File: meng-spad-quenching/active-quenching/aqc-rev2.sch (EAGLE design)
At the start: 289 parts, among them IC1 ADCMP582, IC10 74AHC1G04DBV, IC11 74AHC1G04DBV, IC12 TLV272DGK, IC13 TLV271DBV, IC14 74AHC1G04DBV, IC15 ALD1106, IC16 ALD1107, IC17 74AHC1G04DBV, IC18 LT1534-1, IC19 LT1534-1, IC2 TLV271DBV, IC20 STM32F411RE, IC22 TPS7A3001, IC24 TPS7A4901, IC25 TPS7A4901, IC27 USBLC6-2SC6Y, IC28 MAX572X, IC3 NC7SV74K8X, IC4 TLV272DGK, IC5 NC7WZ16P6X, IC6 LTC1711, IC7 DS1100LU-20+, IC8 LM1117, M1 BSS806N, M2 BSS806N, M3 BSS806N, Q1 IRLML6402TRPBF, Q2 MMBTH81, Q3 MMBTH81, Q5 MMBTH81, Q7 MMBTH81, Q8 MMBTH81, T1 MMBTH10, T2 MMBTH10, T5 MMBTH10, T6 MMBTH10, T7 MMBTH10, T8 MMBTH10, T9 MMBTH10, U1 SN65EPT21DGK, U2 SN65EPT22DGK, X1 CONN_SPAD, X2 CONN_PHOTON_COUNTER, X3 KEYSTONE-7774, X4 KEYSTONE-7774, X5 CONN_SMU, X6 CONN_FORCE_QUENCH, X7 CONN_PULLDN_SENSE, X8 PN61729-S

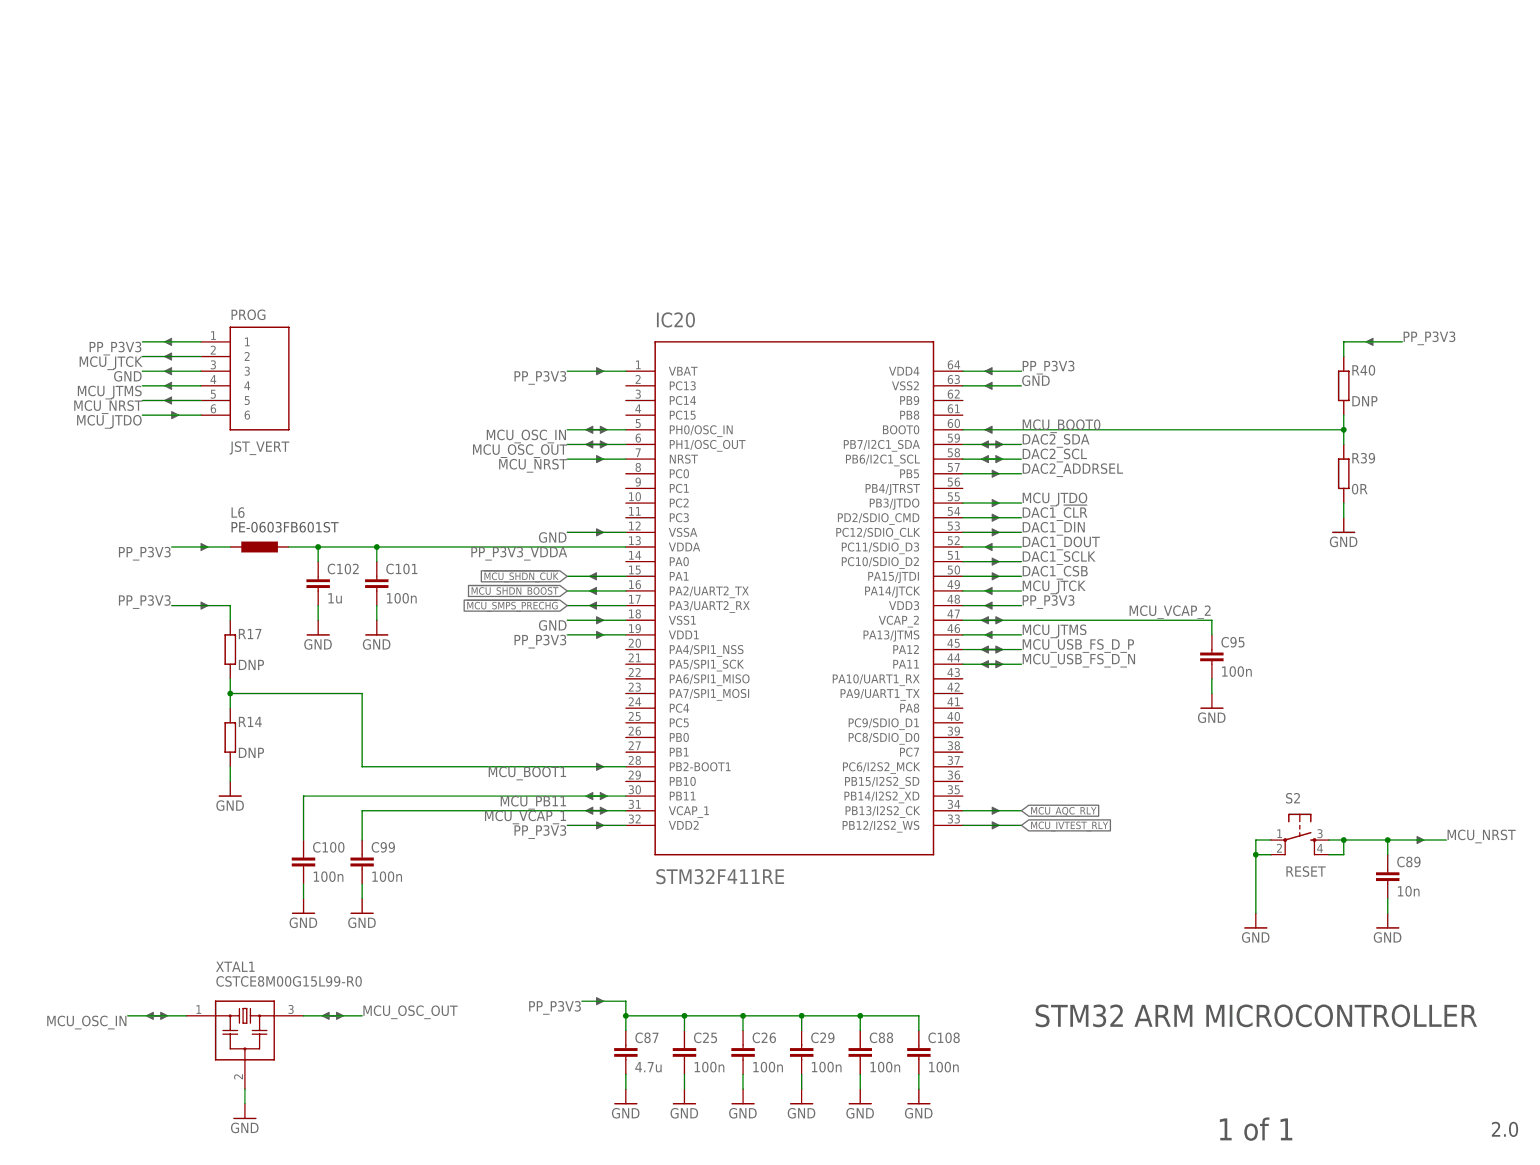
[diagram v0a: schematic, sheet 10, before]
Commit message: Untangled DAC test points
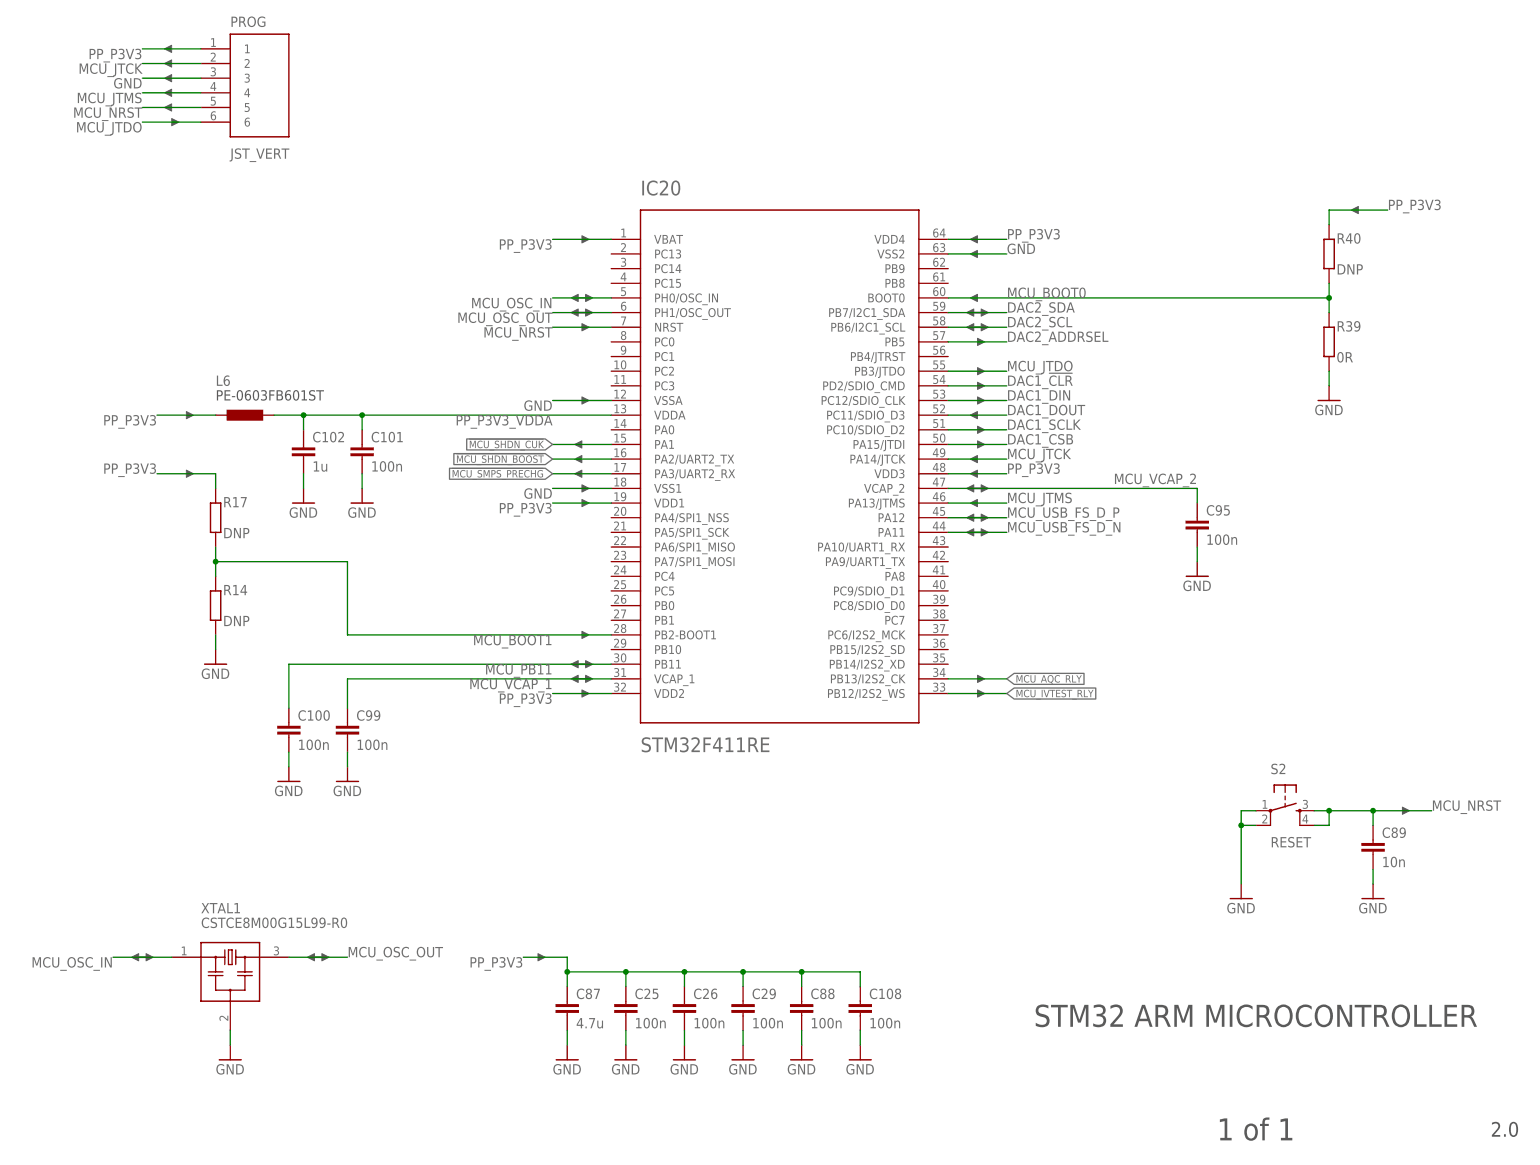
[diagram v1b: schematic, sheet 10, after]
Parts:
- TP10: value VREF_CASCODE_IBIAS -> CASC_IBIAS
- TP11: value VREF_DIAMOND_IBIAS -> DMND_IBIAS
- TP12: value VREF_ONE_SHOT -> ONE_SHOT
- TP15: value VREF_SLEW_UP -> SLEW_UP
- TP16: value VREF_SLEW_DN -> SLEW_DN
- TP17: value VREF_SLEW_MAX -> SLEW_MAX
- TP18: value VREF_DELAY_UP -> DELAY_UP
- TP19: value VREF_DELAY_DN -> DELAY_DN
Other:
- moved on the sheet: C100, C101, C102, C108, C25, C26, C29, C87, C88, C89, C95, C99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

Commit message: Transistor array routing
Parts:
- R37: device resistor:R-EU_R0805 -> resistor:R-EU_R0603
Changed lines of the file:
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@@
 <grid distance="0.1" unitdist="inch" unit="inch" style="lines" multiple="1" display="yes" altdistance="0.01" altunitdist="inch" altunit="inch"/>
 <layers>
-<layer number="1" name="Top" color="4" fill="1" visible="no" active="no"/>
-<layer number="2" name="Route2" color="3" fill="1" visible="no" active="no"/>
-<layer number="3" name="Route3" color="4" fill="3" visible="no" active="no"/>
-<layer number="4" name="Route4" color="1" fill="4" visible="no" active="no"/>
-<layer number="5" name="Route5" color="4" fill="4" visible="no" active="no"/>
-<layer number="6" name="Route6" color="1" fill="8" visible="no" active="no"/>
-<layer number="7" name="Route7" color="4" fill="8" visible="no" active="no"/>
-<layer number="8" name="Route8" color="1" fill="2" visible="no" active="no"/>
-<layer number="9" name="Route9" color="4" fill="2" visible="no" active="no"/>
-<layer number="10" name="Route10" color="1" fill="7" visible="no" active="no"/>
-<layer number="11" name="Route11" color="4" fill="7" visible="no" active="no"/>
-<layer number="12" name="Route12" color="1" fill="5" visible="no" active="no"/>
-<layer number="13" name="Route13" color="4" fill="5" visible="no" active="no"/>
-<layer number="14" name="Route14" color="1" fill="6" visible="no" active="no"/>
-<layer number="15" name="Route15" color="6" fill="1" visible="no" active="no"/>
-<layer number="16" name="Bottom" color="1" fill="1" visible="no" active="no"/>
-<layer number="17" name="Pads" color="2" fill="1" visible="no" active="no"/>
-<layer number="18" name="Vias" color="2" fill="1" visible="no" active="no"/>
-<layer number="19" name="Unrouted" color="6" fill="1" visible="no" active="no"/>
-<layer number="20" name="Dimension" color="15" fill="1" visible="no" active="no"/>
-<layer number="21" name="tPlace" color="7" fill="1" visible="no" active="no"/>
-<layer number="22" name="bPlace" color="7" fill="1" visible="no" active="no"/>
-<layer number="23" name="tOrigins" color="15" fill="1" visible="no" active="no"/>
-<layer number="24" name="bOrigins" color="15" fill="1" visible="no" active="no"/>
-<layer number="25" name="tNames" color="7" fill="1" visible="no" active="no"/>
-<layer number="26" name="bNames" color="7" fill="1" visible="no" active="no"/>
-<layer number="27" name="tValues" color="7" fill="1" visible="no" active="no"/>
-<layer number="28" name="bValues" color="7" fill="1" visible="no" active="no"/>
+<layer number="1" name="Top" color="4" fill="1" visible="yes" active="no"/>
+<layer number="2" name="Route2" color="3" fill="1" visible="yes" active="no"/>
+<layer number="3" name="Route3" color="4" fill="3" visible="yes" active="no"/>
+<layer number="4" name="Route4" color="1" fill="4" visible="yes" active="no"/>
+<layer number="5" name="Route5" color="4" fill="4" visible="yes" active="no"/>
+<layer number="6" name="Route6" color="1" fill="8" visible="yes" active="no"/>
+<layer number="7" name="Route7" color="4" fill="8" visible="yes" active="no"/>
+<layer number="8" name="Route8" color="1" fill="2" visible="yes" active="no"/>
+<layer number="9" name="Route9" color="4" fill="2" visible="yes" active="no"/>
+<layer number="10" name="Route10" color="1" fill="7" visible="yes" active="no"/>
+<layer number="11" name="Route11" color="4" fill="7" visible="yes" active="no"/>
+<layer number="12" name="Route12" color="1" fill="5" visible="yes" active="no"/>
+<layer number="13" name="Route13" color="4" fill="5" visible="yes" active="no"/>
+<layer number="14" name="Route14" color="1" fill="6" visible="yes" active="no"/>
+<layer number="15" name="Route15" color="6" fill="1" visible="yes" active="no"/>
+<layer number="16" name="Bottom" color="1" fill="1" visible="yes" active="no"/>
+<layer number="17" name="Pads" color="2" fill="1" visible="yes" active="no"/>
+<layer number="18" name="Vias" color="2" fill="1" visible="yes" active="no"/>
+<layer number="19" name="Unrouted" color="6" fill="1" visible="yes" active="no"/>
+<layer number="20" name="Dimension" color="15" fill="1" visible="yes" active="no"/>
+<layer number="21" name="tPlace" color="7" fill="1" visible="yes" active="no"/>
+<layer number="22" name="bPlace" color="7" fill="1" visible="yes" active="no"/>
+<layer number="23" name="tOrigins" color="15" fill="1" visible="yes" active="no"/>
+<layer number="24" name="bOrigins" color="15" fill="1" visible="yes" active="no"/>
+<layer number="25" name="tNames" color="7" fill="1" visible="yes" active="no"/>
+<layer number="26" name="bNames" color="7" fill="1" visible="yes" active="no"/>
+<layer number="27" name="tValues" color="7" fill="1" visible="yes" active="no"/>
+<layer number="28" name="bValues" color="7" fill="1" visible="yes" active="no"/>
 <layer number="29" name="tStop" color="7" fill="3" visible="no" active="no"/>
 <layer number="30" name="bStop" color="7" fill="6" visible="no" active="no"/>
@@
 <layer number="35" name="tGlue" color="7" fill="4" visible="no" active="no"/>
 <layer number="36" name="bGlue" color="7" fill="5" visible="no" active="no"/>
-<layer number="37" name="tTest" color="7" fill="1" visible="no" active="no"/>
-<layer number="38" name="bTest" color="7" fill="1" visible="no" active="no"/>
+<layer number="37" name="tTest" color="7" fill="1" visible="yes" active="no"/>
+<layer number="38" name="bTest" color="7" fill="1" visible="yes" active="no"/>
 <layer number="39" name="tKeepout" color="4" fill="11" visible="no" active="no"/>
 <layer number="40" name="bKeepout" color="1" fill="11" visible="no" active="no"/>
@@
 <layer number="44" name="Drills" color="7" fill="1" visible="no" active="no"/>
 <layer number="45" name="Holes" color="7" fill="1" visible="no" active="no"/>
-<layer number="46" name="Milling" color="3" fill="1" visible="no" active="no"/>
-<layer number="47" name="Measures" color="7" fill="1" visible="no" active="no"/>
-<layer number="48" name="Document" color="7" fill="1" visible="no" active="no"/>
-<layer number="49" name="Reference" color="7" fill="1" visible="no" active="no"/>
-<layer number="50" name="dxf" color="7" fill="1" visible="no" active="no"/>
-<layer number="51" name="tDocu" color="7" fill="1" visible="no" active="no"/>
-<layer number="52" name="bDocu" color="7" fill="1" visible="no" active="no"/>
-<layer number="53" name="tPadExt" color="7" fill="1" visible="no" active="no"/>
-<layer number="54" name="bPadExt" color="1" fill="1" visible="no" active="no"/>
-<layer number="56" name="wert" color="7" fill="1" visible="no" active="no"/>
-<layer number="57" name="tCAD" color="7" fill="1" visible="no" active="no"/>
-<layer number="59" name="tCarbon" color="7" fill="1" visible="no" active="no"/>
-<layer number="60" name="bCarbon" color="7" fill="1" visible="no" active="no"/>
+<layer number="46" name="Milling" color="3" fill="1" visible="yes" active="no"/>
+<layer number="47" name="Measures" color="7" fill="1" visible="yes" active="no"/>
+<layer number="48" name="Document" color="7" fill="1" visible="yes" active="no"/>
+<layer number="49" name="Reference" color="7" fill="1" visible="yes" active="no"/>
+<layer number="50" name="dxf" color="7" fill="1" visible="yes" active="no"/>
+<layer number="51" name="tDocu" color="7" fill="1" visible="yes" active="no"/>
+<layer number="52" name="bDocu" color="7" fill="1" visible="yes" active="no"/>
+<layer number="53" name="tPadExt" color="7" fill="1" visible="yes" active="no"/>
+<layer number="54" name="bPadExt" color="1" fill="1" visible="yes" active="no"/>
+<layer number="56" name="wert" color="7" fill="1" visible="yes" active="no"/>
+<layer number="57" name="tCAD" color="7" fill="1" visible="yes" active="no"/>
+<layer number="59" name="tCarbon" color="7" fill="1" visible="yes" active="no"/>
+<layer number="60" name="bCarbon" color="7" fill="1" visible="yes" active="no"/>
 <layer number="90" name="Modules" color="5" fill="1" visible="no" active="no"/>
 <layer number="91" name="Nets" color="2" fill="1" visible="yes" active="yes"/>
@@
 <part name="LED2" library="led" deviceset="LED" device="CHIP-LED0805"/>
 <part name="GND83" library="supply1" deviceset="GND" device=""/>
-<part name="R37" library="resistor" deviceset="R-EU_" device="R0805" value="470R"/>
+<part name="R37" library="resistor" deviceset="R-EU_" device="R0603" value="470R"/>
 <part name="TP12" library="Kramnik's Library" deviceset="KEYSTONE_5000" device="" value="ONE_SHOT"/>
 <part name="TP11" library="Kramnik's Library" deviceset="KEYSTONE_5000" device="" value="DMND_IBIAS"/>

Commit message: Added new SMA conns. w/o dimension edge line
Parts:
- X1, X2, X5, X6, X7: device con-coax:SMA-142-0711-871/876 -> meng:SMA-142-0711-871/876
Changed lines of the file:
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@@
 <part name="GND2" library="supply1" deviceset="GND" device=""/>
 <part name="R15" library="rcl" deviceset="R-EU_" device="R0603" value="10k"/>
-<part name="X1" library="con-coax" deviceset="SMA-" device="142-0711-871/876" value="CONN_SPAD"/>
-<part name="X2" library="con-coax" deviceset="SMA-" device="142-0711-871/876" value="CONN_PHOTON_COUNTER"/>
+<part name="X1" library="meng" deviceset="SMA-" device="142-0711-871/876" value="CONN_SPAD"/>
+<part name="X2" library="meng" deviceset="SMA-" device="142-0711-871/876" value="CONN_PHOTON_COUNTER"/>
 <part name="GND5" library="supply1" deviceset="GND" device=""/>
 <part name="DNP4" library="meng" deviceset="ARROW_1DIR" device=""/>
@@
 <part name="R22" library="rcl" deviceset="R-EU_" device="R0603" value="49R9"/>
 <part name="DNP67" library="meng" deviceset="ARROW_1DIR" device=""/>
-<part name="X6" library="con-coax" deviceset="SMA-" device="142-0711-871/876" value="CONN_FORCE_QUENCH">
+<part name="X6" library="meng" deviceset="SMA-" device="142-0711-871/876" value="CONN_FORCE_QUENCH">
 <attribute name="MF" value="JOHNSON COMPONENTS"/>
 <attribute name="MPN" value="142-0711-871"/>
@@
 <part name="R45" library="rcl" deviceset="R-EU_" device="R0603" value="DNP"/>
 <part name="R46" library="rcl" deviceset="R-EU_" device="R0603" value="0R"/>
-<part name="X7" library="con-coax" deviceset="SMA-" device="142-0711-871/876" value="CONN_PULLDN_SENSE">
+<part name="X7" library="meng" deviceset="SMA-" device="142-0711-871/876" value="CONN_PULLDN_SENSE">
 <attribute name="MF" value="JOHNSON COMPONENTS"/>
 <attribute name="MPN" value="142-0711-871"/>
@@
 <part name="GND161" library="supply1" deviceset="GND" device=""/>
 <part name="GND162" library="supply1" deviceset="GND" device=""/>
-<part name="X5" library="con-coax" deviceset="SMA-" device="142-0711-871/876" value="CONN_SMU"/>
+<part name="X5" library="meng" deviceset="SMA-" device="142-0711-871/876" value="CONN_SMU"/>
 <part name="GND163" library="supply1" deviceset="GND" device=""/>
 <part name="R70" library="rcl" deviceset="R-EU_" device="R0603" value="0R"/>

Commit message: Place & route diamond bias opamp
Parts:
- C82: device rcl:C-EUC0402 -> rcl:C-EUC0603
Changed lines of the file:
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@@
 <part name="GND135" library="supply1" deviceset="GND" device=""/>
 <part name="DNP141" library="meng" deviceset="ARROW_1DIR" device=""/>
-<part name="C82" library="rcl" deviceset="C-EU" device="C0402" value="100n"/>
+<part name="C82" library="rcl" deviceset="C-EU" device="C0603" value="100n"/>
 <part name="GND140" library="supply1" deviceset="GND" device=""/>
 <part name="IC13" library="meng" deviceset="TLV271" device="DBV"/>

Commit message: Work on DAC layout
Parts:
- C50, C51: device rcl:C-EUC0603 -> rcl:C-EUC0402
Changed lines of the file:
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@@
 <part name="Q7" library="transistor-pnp" deviceset="MMBTH81*" device="SMD" technology="LT1" value="MMBTH81"/>
 <part name="R47" library="rcl" deviceset="R-EU_" device="R0603" value="470R"/>
-<part name="C50" library="rcl" deviceset="C-EU" device="C0603" value="100n"/>
-<part name="C51" library="rcl" deviceset="C-EU" device="C0603" value="10n"/>
+<part name="C50" library="rcl" deviceset="C-EU" device="C0402" value="100n"/>
+<part name="C51" library="rcl" deviceset="C-EU" device="C0402" value="10n"/>
 <part name="GND95" library="supply1" deviceset="GND" device=""/>
 <part name="GND96" library="supply1" deviceset="GND" device=""/>

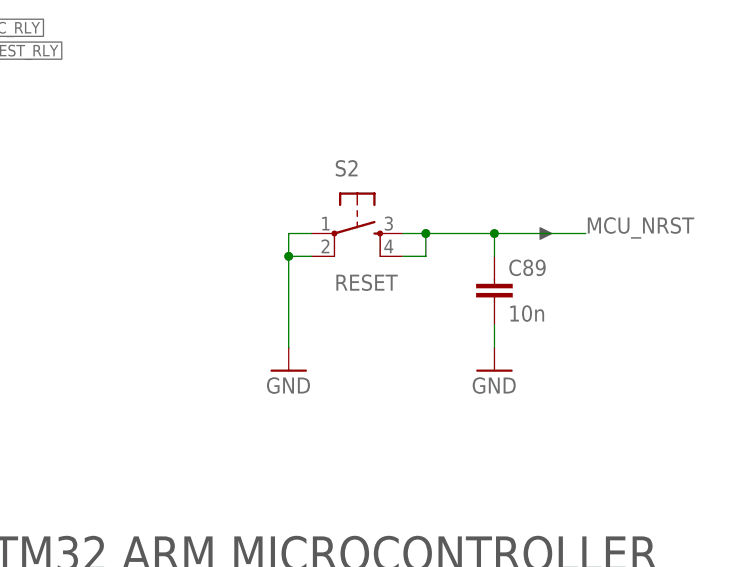
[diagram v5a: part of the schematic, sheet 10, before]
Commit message: started placing one-shot
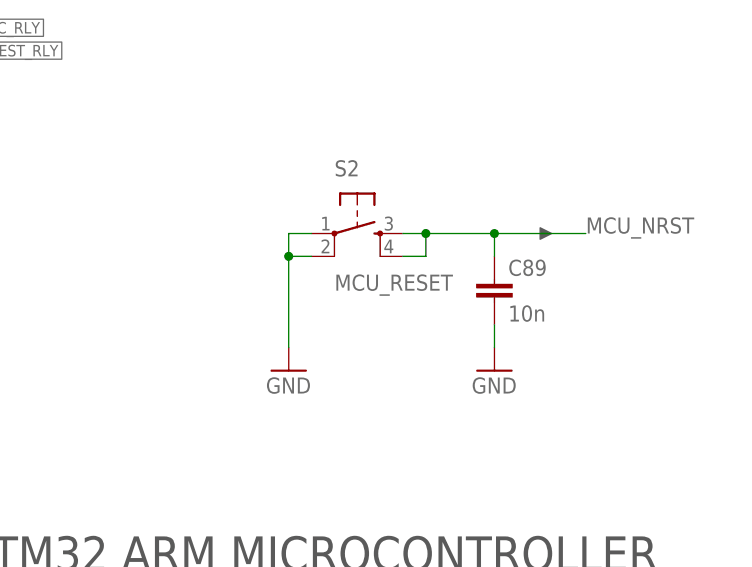
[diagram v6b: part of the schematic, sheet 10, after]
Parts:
- S2: value RESET -> MCU_RESET
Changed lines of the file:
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@@
 <part name="DNP104" library="meng" deviceset="ARROW_1DIR" device=""/>
 <part name="DNP105" library="meng" deviceset="ARROW_1DIR" device=""/>
-<part name="S2" library="Kramnik's Library" deviceset="TAC_SWITCH" device="PTH" value="RESET"/>
+<part name="S2" library="Kramnik's Library" deviceset="TAC_SWITCH" device="PTH" value="MCU_RESET"/>
 <part name="GND73" library="supply1" deviceset="GND" device=""/>
 <part name="C89" library="rcl" deviceset="C-EU" device="C0603" value="10n"/>
